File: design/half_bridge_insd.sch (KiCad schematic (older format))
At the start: 9 parts

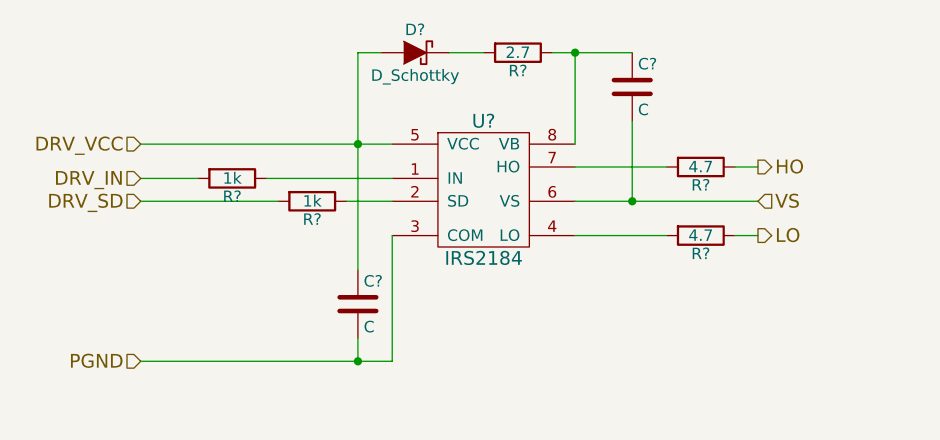
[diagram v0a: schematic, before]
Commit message: Added new drivers and removed the big old one.
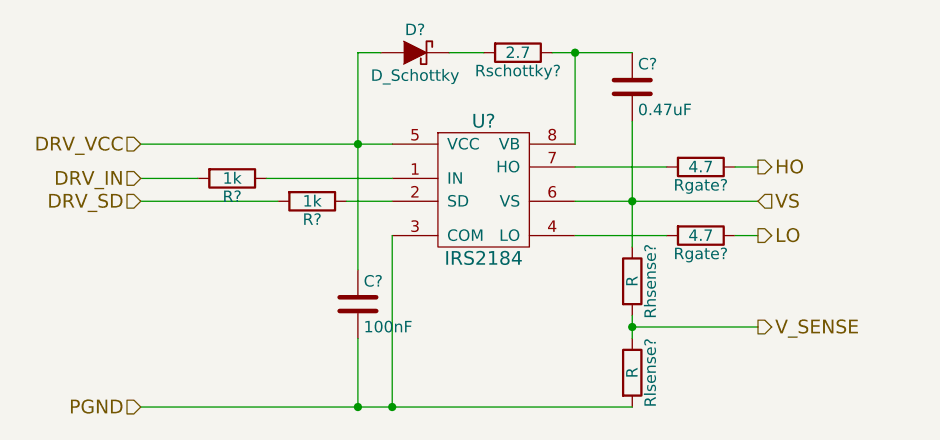
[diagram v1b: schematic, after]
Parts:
- added Rhsense?, Rlsense?: R, symbol R
- C?: value C -> 0.47uF
- C?: value C -> 100nF
- gave numbers to parts that had none: 2
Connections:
- net PGND: now also Rlsense?.2
- net VS: now also Rhsense?.1
- new net V_SENSE: Rhsense?.2, Rlsense?.1
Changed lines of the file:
@@
 $Descr A4 11693 8268
 encoding utf-8
-Sheet 8 8
+Sheet 10 10
 Title ""
 Date ""
@@
 U 1 1 55DDD5BF
 P 5450 3400
+AR Path="/55DB7E47/55DDD5BF" Ref="U?"  Part="1"
+AR Path="/55E59DEF/55DDD5BF" Ref="U?"  Part="1"
+AR Path="/55E6829E/55DDD5BF" Ref="U?"  Part="1"
 F 0 "U?" H 5450 3700 60  0000 C CNN
 F 1 "IRS2184" H 5450 3100 60  0000 C CNN
@@
 Text HLabel 3950 3450 0    60   Input ~ 0
 DRV_SD
-Text HLabel 3950 4150 0    60   Input ~ 0
+Text HLabel 3950 4350 0    60   Input ~ 0
 PGND
 $Comp
@@
 U 1 1 55DE445F
 P 5150 2800
+AR Path="/55DB7E47/55DE445F" Ref="D?"  Part="1"
+AR Path="/55E59DEF/55DE445F" Ref="D?"  Part="1"
+AR Path="/55E6829E/55DE445F" Ref="D?"  Part="1"
 F 0 "D?" H 5150 2900 50  0000 C CNN
 F 1 "D_Schottky" H 5150 2700 50  0000 C CNN
@@
 U 1 1 55DF8324
 P 4350 3350
+AR Path="/55DB7E47/55DF8324" Ref="R?"  Part="1"
+AR Path="/55E59DEF/55DF8324" Ref="R?"  Part="1"
+AR Path="/55E6829E/55DF8324" Ref="R?"  Part="1"
 F 0 "R?" V 4430 3350 50  0000 C CNN
 F 1 "1k" V 4350 3350 50  0000 C CNN
@@
 $EndComp
 $Comp
-L R R?
+L R Rschottky?
 U 1 1 55DF8357
 P 5600 2800
-F 0 "R?" V 5680 2800 50  0000 C CNN
+AR Path="/55DB7E47/55DF8357" Ref="Rschottky?"  Part="1"
+AR Path="/55E59DEF/55DF8357" Ref="Rschottky?"  Part="1"
+AR Path="/55E6829E/55DF8357" Ref="Rschottky?"  Part="1"
+F 0 "Rschottky?" V 5680 2800 50  0000 C CNN
 F 1 "2.7" V 5600 2800 50  0000 C CNN
 F 2 "" V 5530 2800 30  0000 C CNN
@@
 U 1 1 55DF8392
 P 4700 3450
+AR Path="/55DB7E47/55DF8392" Ref="R?"  Part="1"
+AR Path="/55E59DEF/55DF8392" Ref="R?"  Part="1"
+AR Path="/55E6829E/55DF8392" Ref="R?"  Part="1"
 F 0 "R?" V 4780 3450 50  0000 C CNN
 F 1 "1k" V 4700 3450 50  0000 C CNN
@@
 $EndComp
 $Comp
-L R R?
+L R Rgate?
 U 1 1 55DF83B9
 P 6400 3300
-F 0 "R?" V 6480 3300 50  0000 C CNN
+AR Path="/55DB7E47/55DF83B9" Ref="Rgate?"  Part="1"
+AR Path="/55E59DEF/55DF83B9" Ref="Rgate?"  Part="1"
+AR Path="/55E6829E/55DF83B9" Ref="Rgate?"  Part="1"
+F 0 "Rgate?" V 6480 3300 50  0000 C CNN
 F 1 "4.7" V 6400 3300 50  0000 C CNN
 F 2 "" V 6330 3300 30  0000 C CNN
@@
 $EndComp
 $Comp
-L R R?
+L R Rgate?
 U 1 1 55DF843E
 P 6400 3600
-F 0 "R?" V 6480 3600 50  0000 C CNN
+AR Path="/55DB7E47/55DF843E" Ref="Rgate?"  Part="1"
+AR Path="/55E59DEF/55DF843E" Ref="Rgate?"  Part="1"
+AR Path="/55E6829E/55DF843E" Ref="Rgate?"  Part="1"
+F 0 "Rgate?" V 6480 3600 50  0000 C CNN
 F 1 "4.7" V 6400 3600 50  0000 C CNN
 F 2 "" V 6330 3600 30  0000 C CNN
@@
 U 1 1 55DF8D4F
 P 6100 2950
+AR Path="/55DB7E47/55DF8D4F" Ref="C?"  Part="1"
+AR Path="/55E59DEF/55DF8D4F" Ref="C?"  Part="1"
+AR Path="/55E6829E/55DF8D4F" Ref="C?"  Part="1"
 F 0 "C?" H 6125 3050 50  0000 L CNN
-F 1 "C" H 6125 2850 50  0000 L CNN
+F 1 "0.47uF" H 6125 2850 50  0000 L CNN
 F 2 "" H 6138 2800 30  0000 C CNN
 F 3 "" H 6100 2950 60  0000 C CNN
@@
 U 1 1 55DF8D84
 P 4900 3900
+AR Path="/55DB7E47/55DF8D84" Ref="C?"  Part="1"
+AR Path="/55E59DEF/55DF8D84" Ref="C?"  Part="1"
+AR Path="/55E6829E/55DF8D84" Ref="C?"  Part="1"
 F 0 "C?" H 4925 4000 50  0000 L CNN
-F 1 "C" H 4925 3800 50  0000 L CNN
+F 1 "100nF" H 4925 3800 50  0000 L CNN
 F 2 "" H 4938 3750 30  0000 C CNN
 F 3 "" H 4900 3900 60  0000 C CNN
@@
 	5300 2800 5450 2800
 Wire Wire Line
-	3950 4150 5050 4150
-Wire Wire Line
-	4900 4150 4900 4050
-Wire Wire Line
-	5050 4150 5050 3600
-Connection ~ 4900 4150
-Wire Wire Line
 	5750 2800 6100 2800
 Wire Wire Line
@@
 	5850 3450 6650 3450
 Wire Wire Line
-	6100 3450 6100 3100
+	6100 3100 6100 3650
 Wire Wire Line
 	5850 3300 6250 3300
@@
 	6550 3600 6650 3600
 Connection ~ 6100 3450
+Text HLabel 6650 4000 2    60   Output ~ 0
+V_SENSE
+$Comp
+L R Rhsense?
+U 1 1 55E0598B
+P 6100 3800
+AR Path="/55DB7E47/55E0598B" Ref="Rhsense?"  Part="1"
+AR Path="/55E59DEF/55E0598B" Ref="Rhsense?"  Part="1"
+AR Path="/55E6829E/55E0598B" Ref="Rhsense?"  Part="1"
+F 0 "Rhsense?" V 6180 3800 50  0000 C CNN
+F 1 "R" V 6100 3800 50  0000 C CNN
+F 2 "" V 6030 3800 30  0000 C CNN
+F 3 "" H 6100 3800 30  0000 C CNN
+	1    6100 3800
+	1    0    0    -1
+$EndComp
+$Comp
+L R Rlsense?
+U 1 1 55E05BEF
+P 6100 4200
+AR Path="/55DB7E47/55E05BEF" Ref="Rlsense?"  Part="1"
+AR Path="/55E59DEF/55E05BEF" Ref="Rlsense?"  Part="1"
+AR Path="/55E6829E/55E05BEF" Ref="Rlsense?"  Part="1"
+F 0 "Rlsense?" V 6180 4200 50  0000 C CNN
+F 1 "R" V 6100 4200 50  0000 C CNN
+F 2 "" V 6030 4200 30  0000 C CNN
+F 3 "" H 6100 4200 30  0000 C CNN
+	1    6100 4200
+	1    0    0    -1
+$EndComp
+Wire Wire Line
+	3950 4350 6100 4350
+Wire Wire Line
+	4900 4350 4900 4050
+Wire Wire Line
+	5050 4350 5050 3600
+Connection ~ 4900 4350
+Connection ~ 5050 4350
+Wire Wire Line
+	6100 4050 6100 3950
+Wire Wire Line
+	6650 4000 6100 4000
+Connection ~ 6100 4000
 $EndSCHEMATC

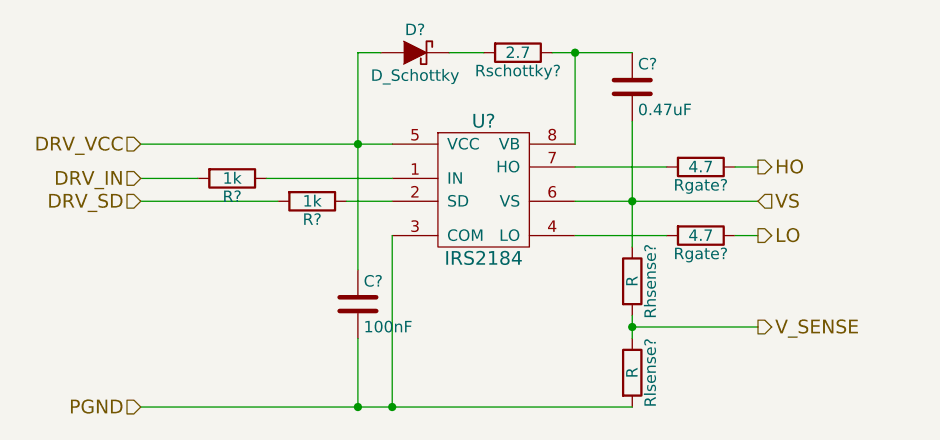
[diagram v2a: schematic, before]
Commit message: First complete draft of the schematics.
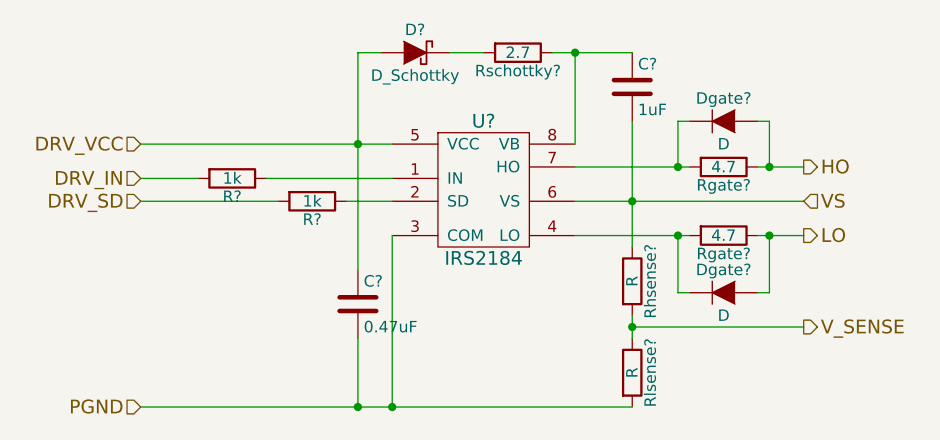
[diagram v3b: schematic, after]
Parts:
- added Dgate? (x2): D, symbol D
- C?: value 0.47uF -> 1uF
- C?: value 100nF -> 0.47uF
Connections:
- net HO: now also Dgate?.2 (A)
- net LO: now also Dgate?.2 (A)
- net at Rgate?.2, U?.4 (LO): now also Dgate?.1 (K)
- net at Rgate?.2, U?.7 (HO): now also Dgate?.1 (K)
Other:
- moved on the sheet: Rgate?
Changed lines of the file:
@@
 $Descr A4 11693 8268
 encoding utf-8
-Sheet 6 10
-Title ""
-Date ""
-Rev ""
+Sheet 6 11
+Title "3-Phase Universal Driver"
+Date "2015-08-27"
+Rev "0.1"
 Comp ""
-Comment1 ""
+Comment1 "Half bridge driver"
 Comment2 ""
 Comment3 ""
@@
 AR Path="/55E59DEF/55DDD5BF" Ref="U?"  Part="1"
 AR Path="/55E6829E/55DDD5BF" Ref="U?"  Part="1"
+AR Path="/55E631D7/55DDD5BF" Ref="U?"  Part="1"
 F 0 "U?" H 5450 3700 60  0000 C CNN
 F 1 "IRS2184" H 5450 3100 60  0000 C CNN
@@
 	1    0    0    -1
 $EndComp
-Text HLabel 6650 3300 2    60   Output ~ 0
+Text HLabel 6850 3300 2    60   Output ~ 0
 HO
-Text HLabel 6650 3600 2    60   Output ~ 0
+Text HLabel 6850 3600 2    60   Output ~ 0
 LO
-Text HLabel 6650 3450 2    60   Input ~ 0
+Text HLabel 6850 3450 2    60   Input ~ 0
 VS
 Text HLabel 3950 3200 0    60   Input ~ 0
@@
 AR Path="/55E59DEF/55DE445F" Ref="D?"  Part="1"
 AR Path="/55E6829E/55DE445F" Ref="D?"  Part="1"
+AR Path="/55E631D7/55DE445F" Ref="D?"  Part="1"
 F 0 "D?" H 5150 2900 50  0000 C CNN
 F 1 "D_Schottky" H 5150 2700 50  0000 C CNN
@@
 AR Path="/55E59DEF/55DF8324" Ref="R?"  Part="1"
 AR Path="/55E6829E/55DF8324" Ref="R?"  Part="1"
+AR Path="/55E631D7/55DF8324" Ref="R?"  Part="1"
 F 0 "R?" V 4430 3350 50  0000 C CNN
 F 1 "1k" V 4350 3350 50  0000 C CNN
@@
 AR Path="/55E59DEF/55DF8357" Ref="Rschottky?"  Part="1"
 AR Path="/55E6829E/55DF8357" Ref="Rschottky?"  Part="1"
+AR Path="/55E631D7/55DF8357" Ref="Rschottky?"  Part="1"
 F 0 "Rschottky?" V 5680 2800 50  0000 C CNN
 F 1 "2.7" V 5600 2800 50  0000 C CNN
@@
 AR Path="/55E59DEF/55DF8392" Ref="R?"  Part="1"
 AR Path="/55E6829E/55DF8392" Ref="R?"  Part="1"
+AR Path="/55E631D7/55DF8392" Ref="R?"  Part="1"
 F 0 "R?" V 4780 3450 50  0000 C CNN
 F 1 "1k" V 4700 3450 50  0000 C CNN
@@
 L R Rgate?
 U 1 1 55DF83B9
-P 6400 3300
+P 6500 3300
 AR Path="/55DB7E47/55DF83B9" Ref="Rgate?"  Part="1"
 AR Path="/55E59DEF/55DF83B9" Ref="Rgate?"  Part="1"
 AR Path="/55E6829E/55DF83B9" Ref="Rgate?"  Part="1"
-F 0 "Rgate?" V 6480 3300 50  0000 C CNN
-F 1 "4.7" V 6400 3300 50  0000 C CNN
-F 2 "" V 6330 3300 30  0000 C CNN
-F 3 "" H 6400 3300 30  0000 C CNN
-	1    6400 3300
+AR Path="/55E631D7/55DF83B9" Ref="Rgate?"  Part="1"
+F 0 "Rgate?" V 6580 3300 50  0000 C CNN
+F 1 "4.7" V 6500 3300 50  0000 C CNN
+F 2 "" V 6430 3300 30  0000 C CNN
+F 3 "" H 6500 3300 30  0000 C CNN
+	1    6500 3300
 	0    1    1    0
 $EndComp
@@
 L R Rgate?
 U 1 1 55DF843E
-P 6400 3600
+P 6500 3600
 AR Path="/55DB7E47/55DF843E" Ref="Rgate?"  Part="1"
 AR Path="/55E59DEF/55DF843E" Ref="Rgate?"  Part="1"
 AR Path="/55E6829E/55DF843E" Ref="Rgate?"  Part="1"
-F 0 "Rgate?" V 6480 3600 50  0000 C CNN
-F 1 "4.7" V 6400 3600 50  0000 C CNN
-F 2 "" V 6330 3600 30  0000 C CNN
-F 3 "" H 6400 3600 30  0000 C CNN
-	1    6400 3600
+AR Path="/55E631D7/55DF843E" Ref="Rgate?"  Part="1"
+F 0 "Rgate?" V 6580 3600 50  0000 C CNN
+F 1 "4.7" V 6500 3600 50  0000 C CNN
+F 2 "" V 6430 3600 30  0000 C CNN
+F 3 "" H 6500 3600 30  0000 C CNN
+	1    6500 3600
 	0    1    1    0
 $EndComp
@@
 AR Path="/55E59DEF/55DF8D4F" Ref="C?"  Part="1"
 AR Path="/55E6829E/55DF8D4F" Ref="C?"  Part="1"
+AR Path="/55E631D7/55DF8D4F" Ref="C?"  Part="1"
 F 0 "C?" H 6125 3050 50  0000 L CNN
-F 1 "0.47uF" H 6125 2850 50  0000 L CNN
+F 1 "1uF" H 6125 2850 50  0000 L CNN
 F 2 "" H 6138 2800 30  0000 C CNN
 F 3 "" H 6100 2950 60  0000 C CNN
@@
 AR Path="/55E59DEF/55DF8D84" Ref="C?"  Part="1"
 AR Path="/55E6829E/55DF8D84" Ref="C?"  Part="1"
+AR Path="/55E631D7/55DF8D84" Ref="C?"  Part="1"
 F 0 "C?" H 4925 4000 50  0000 L CNN
-F 1 "100nF" H 4925 3800 50  0000 L CNN
+F 1 "0.47uF" H 4925 3800 50  0000 L CNN
 F 2 "" H 4938 3750 30  0000 C CNN
 F 3 "" H 4900 3900 60  0000 C CNN
@@
 Connection ~ 5850 2800
 Wire Wire Line
-	5850 3450 6650 3450
+	5850 3450 6850 3450
 Wire Wire Line
 	6100 3100 6100 3650
 Wire Wire Line
-	5850 3300 6250 3300
-Wire Wire Line
-	6550 3300 6650 3300
-Wire Wire Line
-	5850 3600 6250 3600
-Wire Wire Line
-	6550 3600 6650 3600
+	5850 3300 6350 3300
+Wire Wire Line
+	5850 3600 6350 3600
 Connection ~ 6100 3450
-Text HLabel 6650 4000 2    60   Output ~ 0
+Text HLabel 6850 4000 2    60   Output ~ 0
 V_SENSE
 $Comp
@@
 AR Path="/55E59DEF/55E0598B" Ref="Rhsense?"  Part="1"
 AR Path="/55E6829E/55E0598B" Ref="Rhsense?"  Part="1"
+AR Path="/55E631D7/55E0598B" Ref="Rhsense?"  Part="1"
 F 0 "Rhsense?" V 6180 3800 50  0000 C CNN
 F 1 "R" V 6100 3800 50  0000 C CNN
@@
 AR Path="/55E59DEF/55E05BEF" Ref="Rlsense?"  Part="1"
 AR Path="/55E6829E/55E05BEF" Ref="Rlsense?"  Part="1"
+AR Path="/55E631D7/55E05BEF" Ref="Rlsense?"  Part="1"
 F 0 "Rlsense?" V 6180 4200 50  0000 C CNN
 F 1 "R" V 6100 4200 50  0000 C CNN
@@
 	6100 4050 6100 3950
 Wire Wire Line
-	6650 4000 6100 4000
+	6100 4000 6850 4000
 Connection ~ 6100 4000
+$Comp
+L D Dgate?
+U 1 1 55E9685F
+P 6500 3100
+F 0 "Dgate?" H 6500 3200 50  0000 C CNN
+F 1 "D" H 6500 3000 50  0000 C CNN
+F 2 "" H 6500 3100 60  0000 C CNN
+F 3 "" H 6500 3100 60  0000 C CNN
+	1    6500 3100
+	1    0    0    -1
+$EndComp
+Wire Wire Line
+	6350 3100 6300 3100
+Wire Wire Line
+	6300 3100 6300 3300
+Connection ~ 6300 3300
+$Comp
+L D Dgate?
+U 1 1 55E96991
+P 6500 3850
+F 0 "Dgate?" H 6500 3950 50  0000 C CNN
+F 1 "D" H 6500 3750 50  0000 C CNN
+F 2 "" H 6500 3850 60  0000 C CNN
+F 3 "" H 6500 3850 60  0000 C CNN
+	1    6500 3850
+	1    0    0    -1
+$EndComp
+Wire Wire Line
+	6650 3300 6850 3300
+Wire Wire Line
+	6650 3100 6700 3100
+Wire Wire Line
+	6700 3100 6700 3300
+Connection ~ 6700 3300
+Wire Wire Line
+	6650 3600 6850 3600
+Wire Wire Line
+	6650 3850 6700 3850
+Wire Wire Line
+	6700 3850 6700 3600
+Connection ~ 6700 3600
+Wire Wire Line
+	6350 3850 6300 3850
+Wire Wire Line
+	6300 3850 6300 3600
+Connection ~ 6300 3600
 $EndSCHEMATC
